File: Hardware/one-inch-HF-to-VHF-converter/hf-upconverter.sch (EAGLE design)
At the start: 14 parts, among them IC1 74VHC4053, T1 PT61018PEL

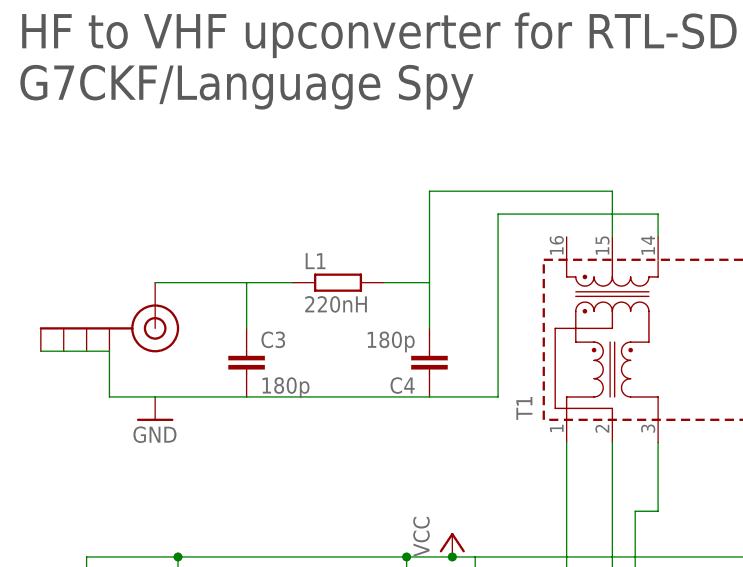
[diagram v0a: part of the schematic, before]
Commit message: Small schematic symbol change in HF upconverter
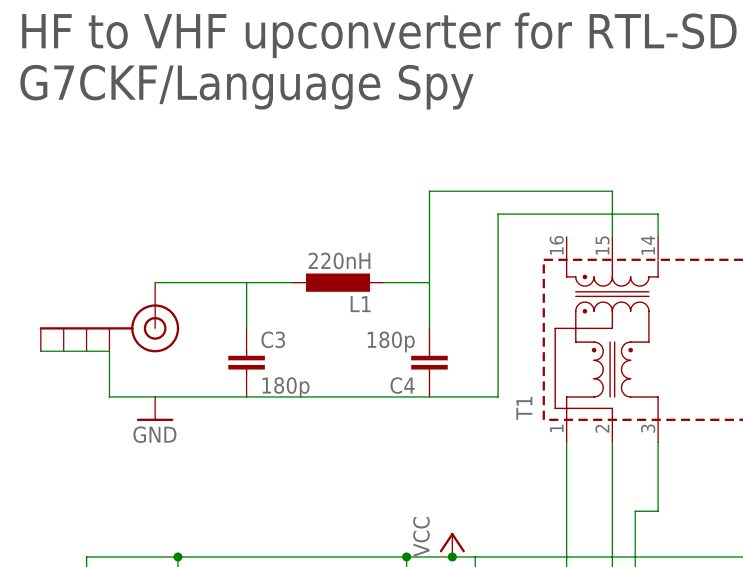
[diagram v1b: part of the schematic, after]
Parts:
- L1: device rcl:R-EU_R1206 -> L1206:L-EU
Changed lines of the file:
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@@
 <part name="SUPPLY1" library="supply2" deviceset="VEE" device=""/>
 <part name="GND4" library="supply1" deviceset="GND" device=""/>
-<part name="L1" library="rcl" deviceset="R-EU_" device="R1206" value="220nH"/>
+<part name="L1" library="L1206" deviceset="L-EU" device="" value="220nH"/>
 <part name="C3" library="rcl" deviceset="C-EU" device="C0805" value="180p"/>
 <part name="C4" library="rcl" deviceset="C-EU" device="C0805" value="180p"/>
@@
 <instance part="SUPPLY1" gate="G$1" x="101.6" y="22.86"/>
 <instance part="GND4" gate="1" x="101.6" y="17.78"/>
-<instance part="L1" gate="G$1" x="83.82" y="109.22"/>
+<instance part="L1" gate="G$1" x="83.82" y="109.22" rot="R90"/>
 <instance part="C3" gate="G$1" x="73.66" y="101.6"/>
 <instance part="C4" gate="G$1" x="93.98" y="99.06" rot="R180"/>
